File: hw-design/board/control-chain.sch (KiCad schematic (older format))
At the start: 17 parts, among them J1 CC_INPUT, J2 CC_OUTPUT, Q2 BSS84, Q3 BSS84, Q4 IRFML8244TRPBF, U1 ISL83491

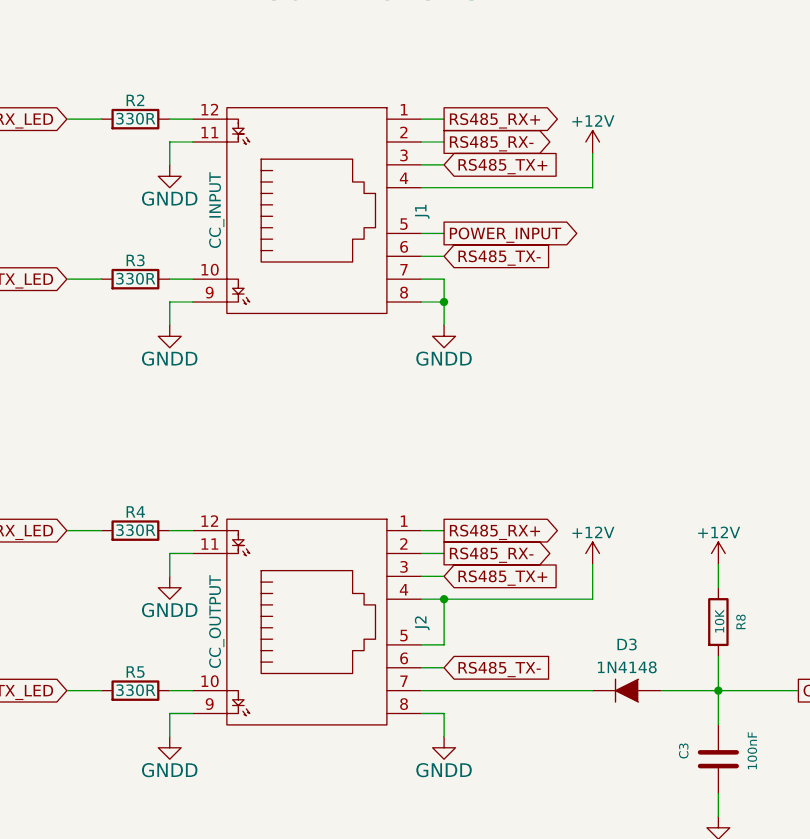
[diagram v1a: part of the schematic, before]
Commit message: connect all voltage inputs pins
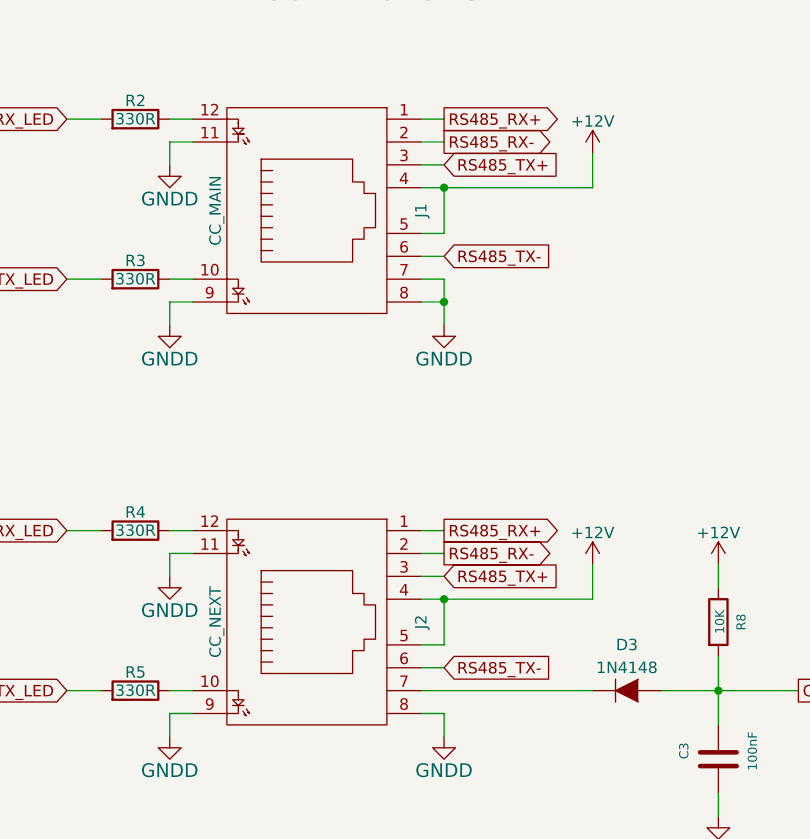
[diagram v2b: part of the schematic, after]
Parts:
- J1: value CC_INPUT -> CC_MAIN
- J2: value CC_OUTPUT -> CC_NEXT
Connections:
- net POWER_INPUT is gone; now on net +12V: J1.5
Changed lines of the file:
@@
 P 3150 2000
 F 0 "J1" H 3150 1500 50  0000 C CNN
-F 1 "CC_INPUT" H 3150 2400 50  0000 C CNN
+F 1 "CC_MAIN" H 3150 2400 50  0000 C CNN
 F 2 "Connect:RJHSE538X" H 3150 1950 60  0001 C CNN
 F 3 "" H 3150 1950 60  0000 C CNN
@@
 P 3150 3800
 F 0 "J2" H 3150 3300 50  0000 C CNN
-F 1 "CC_OUTPUT" H 3150 4200 50  0000 C CNN
+F 1 "CC_NEXT" H 3150 4200 50  0000 C CNN
 F 2 "Connect:RJHSE538X" H 3150 3750 60  0001 C CNN
 F 3 "" H 3150 3750 60  0000 C CNN
@@
 Text GLabel 3750 3500 2    50   Output ~ 0
 RS485_RX-
-Text GLabel 3750 2100 2    50   Output ~ 0
-POWER_INPUT
 Text GLabel 5300 4100 2    50   Output ~ 0
 CC_OUTPUT_DET
@@
 	4400 3700 4400 3550
 Wire Wire Line
-	3650 3900 3750 3900
-Wire Wire Line
-	3750 3900 3750 3700
-Wire Wire Line
 	8300 5250 8300 5150
 Wire Wire Line
@@
 Connection ~ 3750 2400
 Connection ~ 4950 4100
-Connection ~ 3750 3700
 Connection ~ 7850 3150
 Connection ~ 8150 1650
@@
 Wire Wire Line
 	4150 5800 4150 5900
+Wire Wire Line
+	3650 3900 3750 3900
+Wire Wire Line
+	3750 3900 3750 3700
+Connection ~ 3750 3700
+Wire Wire Line
+	3750 2100 3750 1900
+Connection ~ 3750 1900
 $EndSCHEMATC

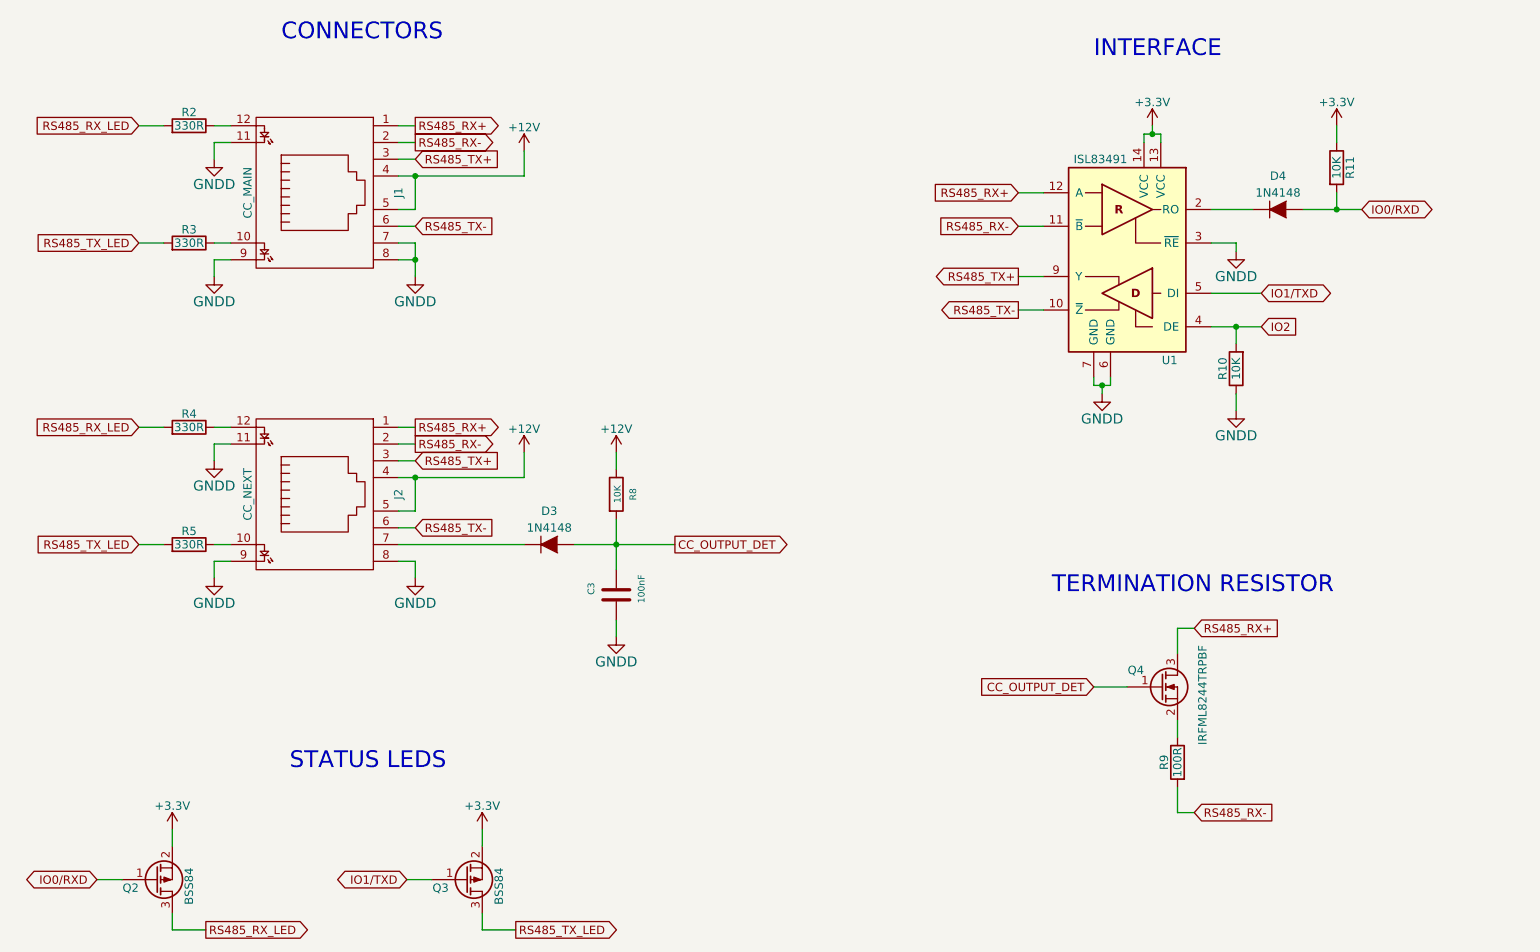
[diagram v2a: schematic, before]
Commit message: change RJ45 connector
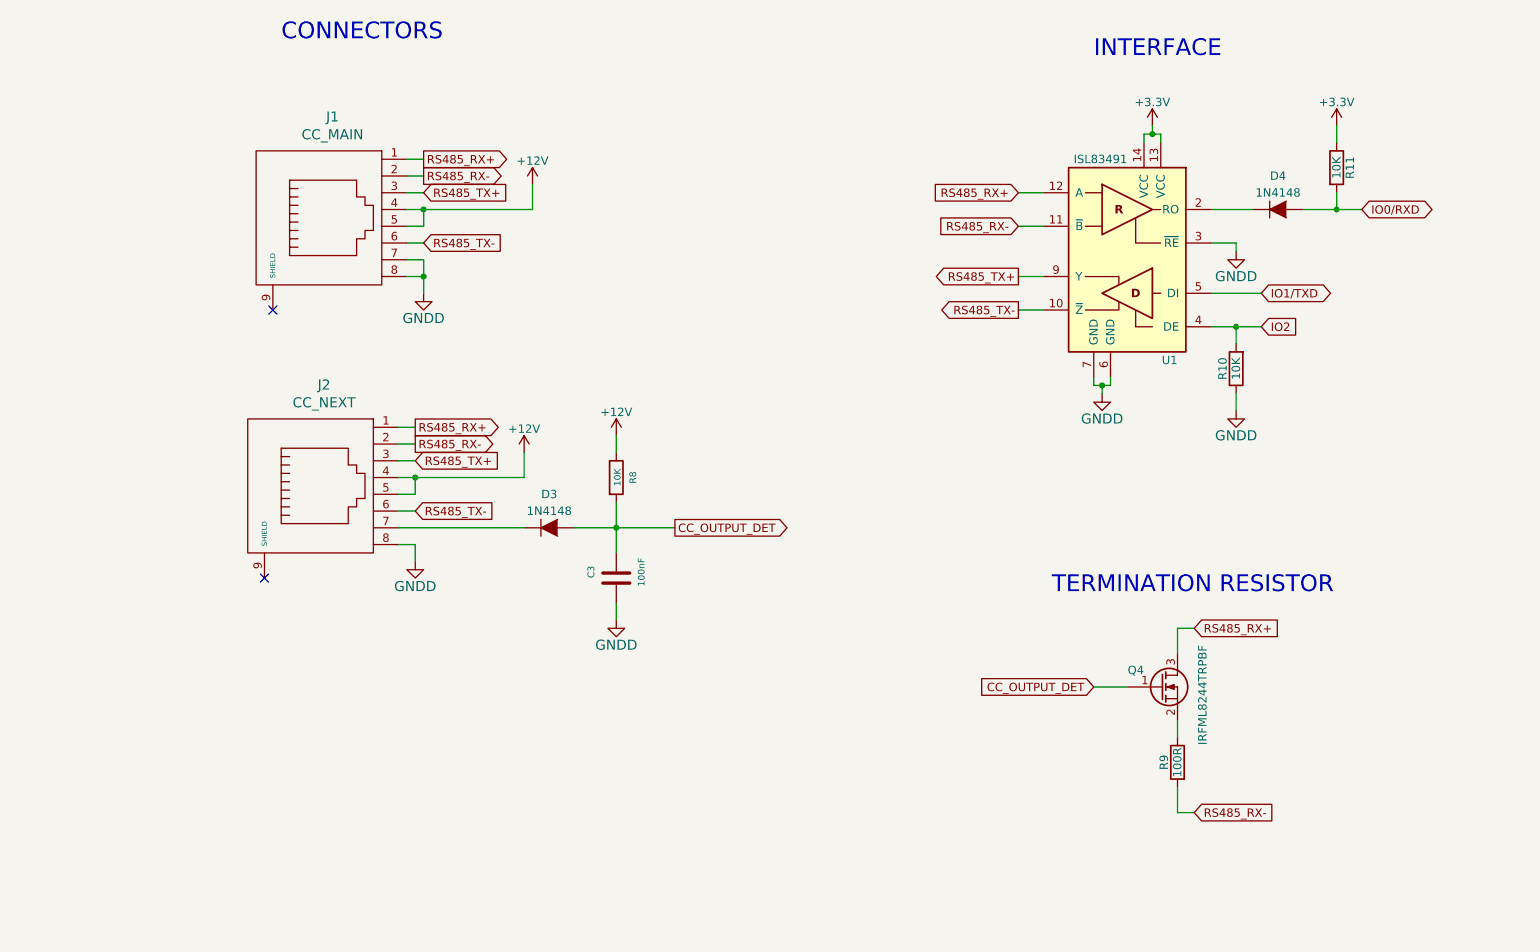
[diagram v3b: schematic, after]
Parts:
- removed J1: CC_MAIN, Connect:RJHSE538X, symbol RJ45_LEDS
- removed J2: CC_NEXT, Connect:RJHSE538X, symbol RJ45_LEDS
- removed Q2, Q3: BSS84, Housings_SOT-23_SOT-143_TSOT-6:SOT-23, symbol Q_PMOS_GSD
- removed R2, R3, R4, R5: 330R, Resistors_SMD:R_0603, symbol R
- added J1: CC_MAIN, local-footprints:54602-908LF, symbol RJ45
- added J2: CC_NEXT, local-footprints:54602-908LF, symbol RJ45
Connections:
- net +12V: now also J1.4, J1.5, J2.4, J2.5
- net GNDD: now also J1.7, J1.8, J2.8
- net RS485_RX+: now also J1.1, J2.1
- net RS485_RX-: now also J1.2, J2.2
- net RS485_TX+: now also J1.3, J2.3
- net RS485_TX-: now also J1.6, J2.6
- net at D3.1 (K): now also J2.7
- no-connect marks 0 -> 2
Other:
- note removed: "STATUS LEDS"
- moved on the sheet: C3, D3, R8

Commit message: add enable circuit for RE pin
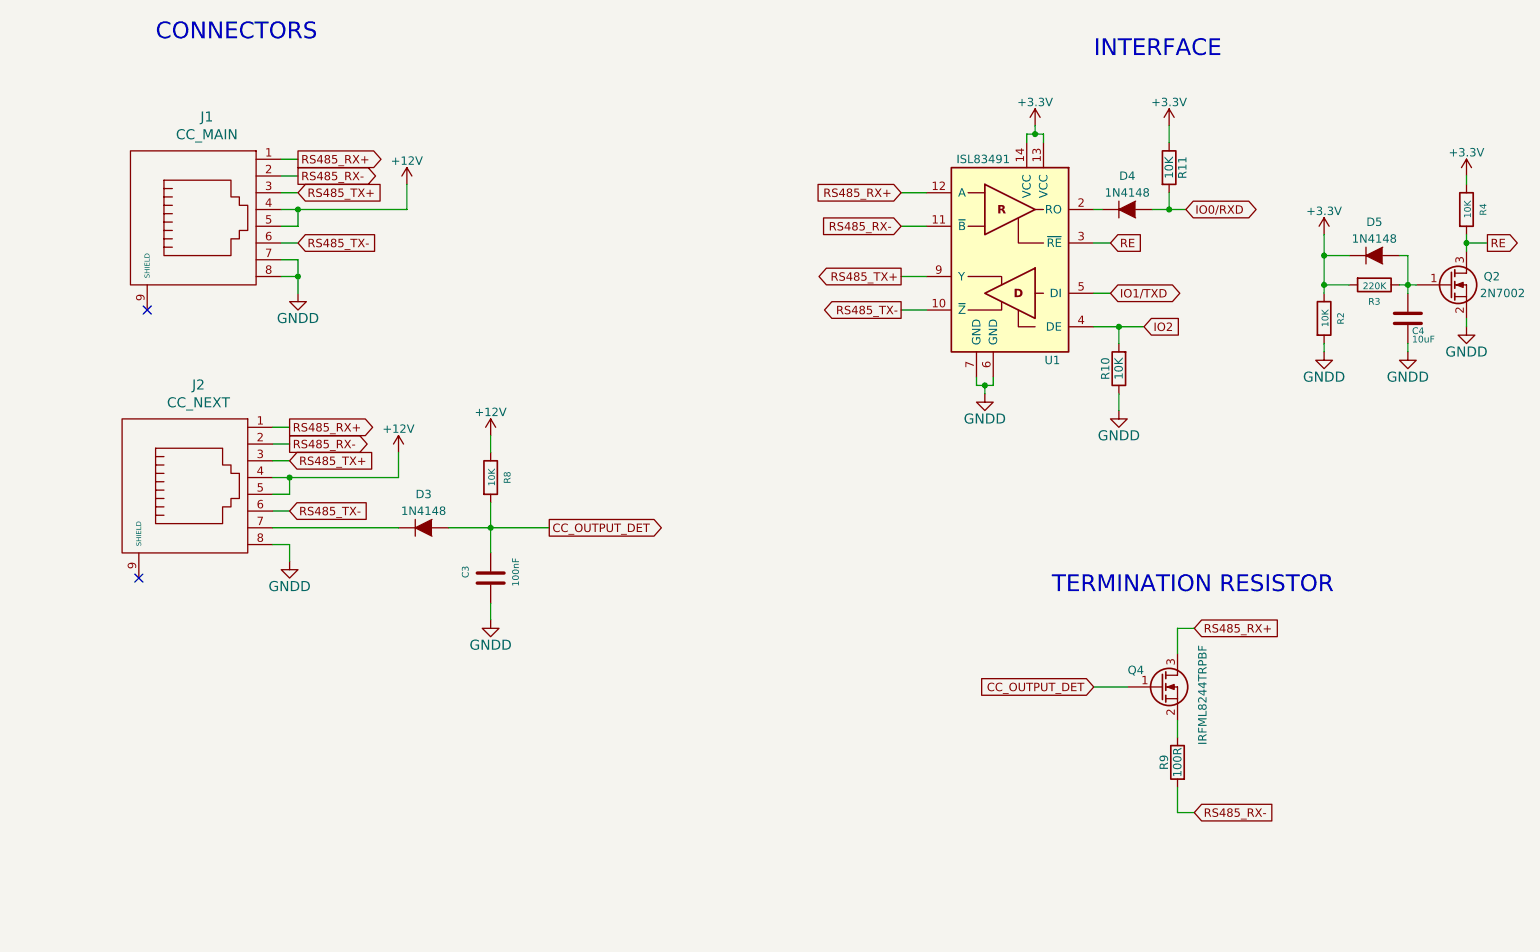
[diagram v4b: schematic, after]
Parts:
- added C4: 10uF, Capacitors_SMD:C_0603, symbol C
- added D5: 1N4148, Diodes_SMD:SOD-323, symbol D
- added Q2: 2N7002, Housings_SOT-23_SOT-143_TSOT-6:SOT-23, symbol Q_NMOS_GSD
- added R2, R4: 10K, Resistors_SMD:R_0603, symbol R
- added R3: 220K, Resistors_SMD:R_0603, symbol R
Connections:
- net +3V3: now also D5.1 (K), R2.1, R3.2, R4.1
- net GNDD: now also C4.2, Q2.2 (S), R2.2; no longer U1.3 (~RE)
- new net: C4.1, D5.2 (A), Q2.1 (G), R3.1
- new net RE: Q2.3 (D), R4.2, U1.3 (~RE)
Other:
- moved on the sheet: C3, D3, D4, J1, J2, R10, R11, R8, U1
